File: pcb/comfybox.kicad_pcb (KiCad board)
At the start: 2 copper layers, 0 parts

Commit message: finished pcb without oled
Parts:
- added DOWN1: SW_CHOC, Kailh:Kailh_socket_PG1350_optional, F.Cu at (85.1, 61.3)
- added K1: SW_CHOC, Kailh:Kailh_socket_PG1350_optional, F.Cu at (155.0, 98.3)
- added K2: SW_CHOC, Kailh:Kailh_socket_PG1350_optional, F.Cu at (175.9, 78.7)
- added K3: SW_CHOC, Kailh:Kailh_socket_PG1350_optional, F.Cu at (204.0, 71.7)
- added K4: SW_CHOC, Kailh:Kailh_socket_PG1350_optional, F.Cu at (232.9, 71.7)
- added LEFT1: SW_CHOC, Kailh:Kailh_socket_PG1350_optional, F.Cu at (57.0, 54.3)
- added OPT1: SW_Push, Button_Switch_THT:SW_PUSH_6mm, F.Cu at (42.8, 35.2)
- added OPT2: SW_Push, Button_Switch_THT:SW_PUSH_6mm, F.Cu at (54.8, 35.2)
- added OPT3: SW_Push, Button_Switch_THT:SW_PUSH_6mm, F.Cu at (66.8, 35.2)
- added OPT4: SW_Push, Button_Switch_THT:SW_PUSH_6mm, F.Cu at (78.8, 35.2)
- added OPT5: SW_Push, Button_Switch_THT:SW_PUSH_6mm, F.Cu at (90.8, 35.2)
- added P1: SW_CHOC, Kailh:Kailh_socket_PG1350_optional, F.Cu at (150.0, 70.2)
- added P2: SW_CHOC, Kailh:Kailh_socket_PG1350_optional, F.Cu at (170.9, 50.6)
- added P3: SW_CHOC, Kailh:Kailh_socket_PG1350_optional, F.Cu at (199.0, 43.5)
- added P4: SW_CHOC, Kailh:Kailh_socket_PG1350_optional, F.Cu at (227.9, 43.5)
- added RIGHT1: SW_CHOC, Kailh:Kailh_socket_PG1350_optional, F.Cu at (106.0, 81.0)
- added RPZ1: RP2040-Zero, RP2040-Zero:RP2040-Zero, F.Cu at (130.1, 35.0)
- added UP1: SW_CHOC, Kailh:Kailh_socket_PG1350_optional, F.Cu at (106.0, 130.0)
- added UP2: SW_CHOC, Kailh:Kailh_socket_PG1350_optional, F.Cu at (150.0, 130.0)
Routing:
- net K4: track 0.00 -> 141.3 mm
- net UP L: track 0.00 -> 113.2 mm
- net UP R: track 0.00 -> 112.4 mm
- net P4: track 0.00 -> 109.9 mm
- net K3: track 0.00 -> 104.2 mm
- net START: track 0.00 -> 87.7 mm
- net LEFT: track 0.00 -> 83.5 mm
- net K1: track 0.00 -> 79.8 mm
- net P3: track 0.00 -> 79.0 mm
- net K2: track 0.00 -> 77.8 mm
- net SELECT: track 0.00 -> 74.7 mm
- net RIGHT: track 0.00 -> 63.2 mm
- net HOME: track 0.00 -> 61.6 mm
- net DOWN: track 0.00 -> 61.6 mm
- net P2: track 0.00 -> 51.6 mm
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- added copper zone on B.Cu, net GND
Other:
- board outline added: 242 x 138 mm

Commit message: add oled
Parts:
- added OLED1: SSD1306, SSD1306:128x64OLED, F.Cu at (135.0, 102.0)
- moved OPT1 19.0 mm to (61.8, 35.2)
- moved OPT2 19.0 mm to (73.8, 35.2)
- moved OPT3 19.0 mm to (85.8, 35.2)
- moved OPT4 19.0 mm to (97.8, 35.2)
- moved OPT5 19.0 mm to (109.8, 35.2)
- moved K1 12.0 mm to (167.0, 98.3)
- moved K2 12.0 mm to (187.9, 78.7)
- moved K3 12.0 mm to (216.0, 71.7)
- moved K4 12.0 mm to (244.9, 71.7)
- moved P1 12.0 mm to (162.0, 70.2)
- moved P2 12.0 mm to (182.9, 50.6)
- moved P3 12.0 mm to (211.0, 43.5)
- moved P4 12.0 mm to (239.9, 43.5)
- moved UP2 12.0 mm to (162.0, 130.0)
- moved RPZ1 4.91 mm to (135.0, 35.0)
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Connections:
- RPZ1 pad 21: +3.3V -> 3V3
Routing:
- net OLED SDA: track 0.00 -> 74.9 mm, vias 0 -> 4
- net 3V3: track 0.00 -> 73.5 mm, vias 0 -> 4
- net OLED SCL: track 0.00 -> 71.3 mm, vias 0 -> 4
- net LEFT: track 83.5 -> 105.6 mm
- net K4: track 141.3 -> 163.1 mm
- net P4: track 109.9 -> 131.0 mm
- net K3: track 104.2 -> 124.9 mm
- net K1: track 79.8 -> 98.9 mm
- net UP L: track 113.2 -> 131.4 mm
- net UP R: track 112.4 -> 129.0 mm
- net RIGHT: track 63.2 -> 79.6 mm
- net P3: track 79.0 -> 95.3 mm
- net P1: track 51.4 -> 67.1 mm
- net K2: track 77.8 -> 92.3 mm
- net START: track 87.7 -> 73.6 mm
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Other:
- outline, holes or cut-outs redrawn

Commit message: adjust tracing
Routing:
- net P1: track 67.1 -> 71.7 mm
- net UP R: track 129.0 -> 126.7 mm
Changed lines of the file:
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@@
   (gr_line (start 142 23) (end 257 23) (layer "Edge.Cuts") (width 0.1))
   (gr_line (start 128 44.485516) (end 128 23) (layer "Edge.Cuts") (width 0.1))
-  (segment (start 144 76) (end 144 45.305516) (width 0.25) (layer "F.Cu") (net 1))
-  (segment (start 150 82) (end 144 76) (width 0.25) (layer "F.Cu") (net 1))
-  (segment (start 156.095571 82) (end 150 82) (width 0.25) (layer "F.Cu") (net 1))
+  (segment (start 147.272792 81.5) (end 139.518198 73.745406) (width 0.25) (layer "F.Cu") (net 1))
+  (segment (start 144 46.5) (end 144 45.305516) (width 0.25) (layer "F.Cu") (net 1))
   (segment (start 144 45.305516) (end 144.16 45.145516) (width 0.25) (layer "F.Cu") (net 1))
-  (segment (start 162.00027 76.095301) (end 156.095571 82) (width 0.25) (layer "F.Cu") (net 1))
+  (segment (start 139.518198 50.981802) (end 144 46.5) (width 0.25) (layer "F.Cu") (net 1))
+  (segment (start 156.595571 81.5) (end 147.272792 81.5) (width 0.25) (layer "F.Cu") (net 1))
+  (segment (start 162.00027 76.095301) (end 156.595571 81.5) (width 0.25) (layer "F.Cu") (net 1))
+  (segment (start 139.518198 73.745406) (end 139.518198 50.981802) (width 0.25) (layer "F.Cu") (net 1))
   (segment (start 158.76027 72.820301) (end 162.03527 76.095301) (width 0.25) (layer "B.Cu") (net 1))
   (segment (start 158.76027 64.245301) (end 158.76027 72.820301) (width 0.25) (layer "B.Cu") (net 1))
@@
   (segment (start 236.631082 46.172382) (end 239.906082 49.447382) (width 0.25) (layer "B.Cu") (net 5))
   (segment (start 236.631082 37.597382) (end 236.631082 46.172382) (width 0.25) (layer "B.Cu") (net 5))
-  (segment (start 150 84) (end 140 74) (width 0.25) (layer "F.Cu") (net 6))
-  (segment (start 140 74) (end 140 46.765516) (width 0.25) (layer "F.Cu") (net 6))
-  (segment (start 140 46.765516) (end 140.08 46.685516) (width 0.25) (layer "F.Cu") (net 6))
-  (segment (start 152 110) (end 150 108) (width 0.25) (layer "F.Cu") (net 6))
+  (segment (start 150 84.863604) (end 139.068198 73.931802) (width 0.25) (layer "F.Cu") (net 6))
+  (segment (start 152.5 110) (end 150 107.5) (width 0.25) (layer "F.Cu") (net 6))
   (segment (start 167.00027 104.233869) (end 161.234139 110) (width 0.25) (layer "F.Cu") (net 6))
-  (segment (start 161.234139 110) (end 152 110) (width 0.25) (layer "F.Cu") (net 6))
-  (segment (start 150 108) (end 150 84) (width 0.25) (layer "F.Cu") (net 6))
+  (segment (start 139.068198 50.511802) (end 140.08 49.5) (width 0.25) (layer "F.Cu") (net 6))
+  (segment (start 161.234139 110) (end 152.5 110) (width 0.25) (layer "F.Cu") (net 6))
+  (segment (start 150 107.5) (end 150 84.863604) (width 0.25) (layer "F.Cu") (net 6))
+  (segment (start 140.08 49.5) (end 140.08 46.685516) (width 0.25) (layer "F.Cu") (net 6))
+  (segment (start 139.068198 73.931802) (end 139.068198 50.5) (width 0.25) (layer "F.Cu") (net 6))
   (segment (start 163.76027 100.958869) (end 167.03527 104.233869) (width 0.25) (layer "B.Cu") (net 6))
   (segment (start 163.76027 92.383869) (end 163.76027 100.958869) (width 0.25) (layer "B.Cu") (net 6))
@@
   (segment (start 103.725 132.625) (end 107 135.9) (width 0.25) (layer "B.Cu") (net 13))
   (segment (start 103.725 124.05) (end 103.725 132.625) (width 0.25) (layer "B.Cu") (net 13))
-  (segment (start 162 135.9) (end 154.9 143) (width 0.25) (layer "F.Cu") (net 14))
-  (segment (start 149 85) (end 137.54 73.54) (width 0.25) (layer "F.Cu") (net 14))
-  (segment (start 154.9 143) (end 151 143) (width 0.25) (layer "F.Cu") (net 14))
-  (segment (start 137.54 73.54) (end 137.54 46.685516) (width 0.25) (layer "F.Cu") (net 14))
-  (segment (start 149 141) (end 149 85) (width 0.25) (layer "F.Cu") (net 14))
-  (segment (start 151 143) (end 149 141) (width 0.25) (layer "F.Cu") (net 14))
+  (segment (start 149.5 139.5) (end 149.5 85) (width 0.25) (layer "F.Cu") (net 14))
+  (segment (start 137.5 46.725516) (end 137.54 46.685516) (width 0.25) (layer "F.Cu") (net 14))
+  (segment (start 162 135.9) (end 156.4 141.5) (width 0.25) (layer "F.Cu") (net 14))
+  (segment (start 149.5 85) (end 138.5 74) (width 0.25) (layer "F.Cu") (net 14))
+  (segment (start 138.5 74) (end 138.5 50.5) (width 0.25) (layer "F.Cu") (net 14))
+  (segment (start 156.4 141.5) (end 151.5 141.5) (width 0.25) (layer "F.Cu") (net 14))
+  (segment (start 138.5 50.5) (end 137.5 49.5) (width 0.25) (layer "F.Cu") (net 14))
+  (segment (start 151.5 141.5) (end 149.5 139.5) (width 0.25) (layer "F.Cu") (net 14))
+  (segment (start 137.5 49.5) (end 137.5 46.725516) (width 0.25) (layer "F.Cu") (net 14))
   (segment (start 158.725 132.625) (end 162 135.9) (width 0.25) (layer "B.Cu") (net 14))
   (segment (start 158.725 124.05) (end 158.725 132.625) (width 0.25) (layer "B.Cu") (net 14))

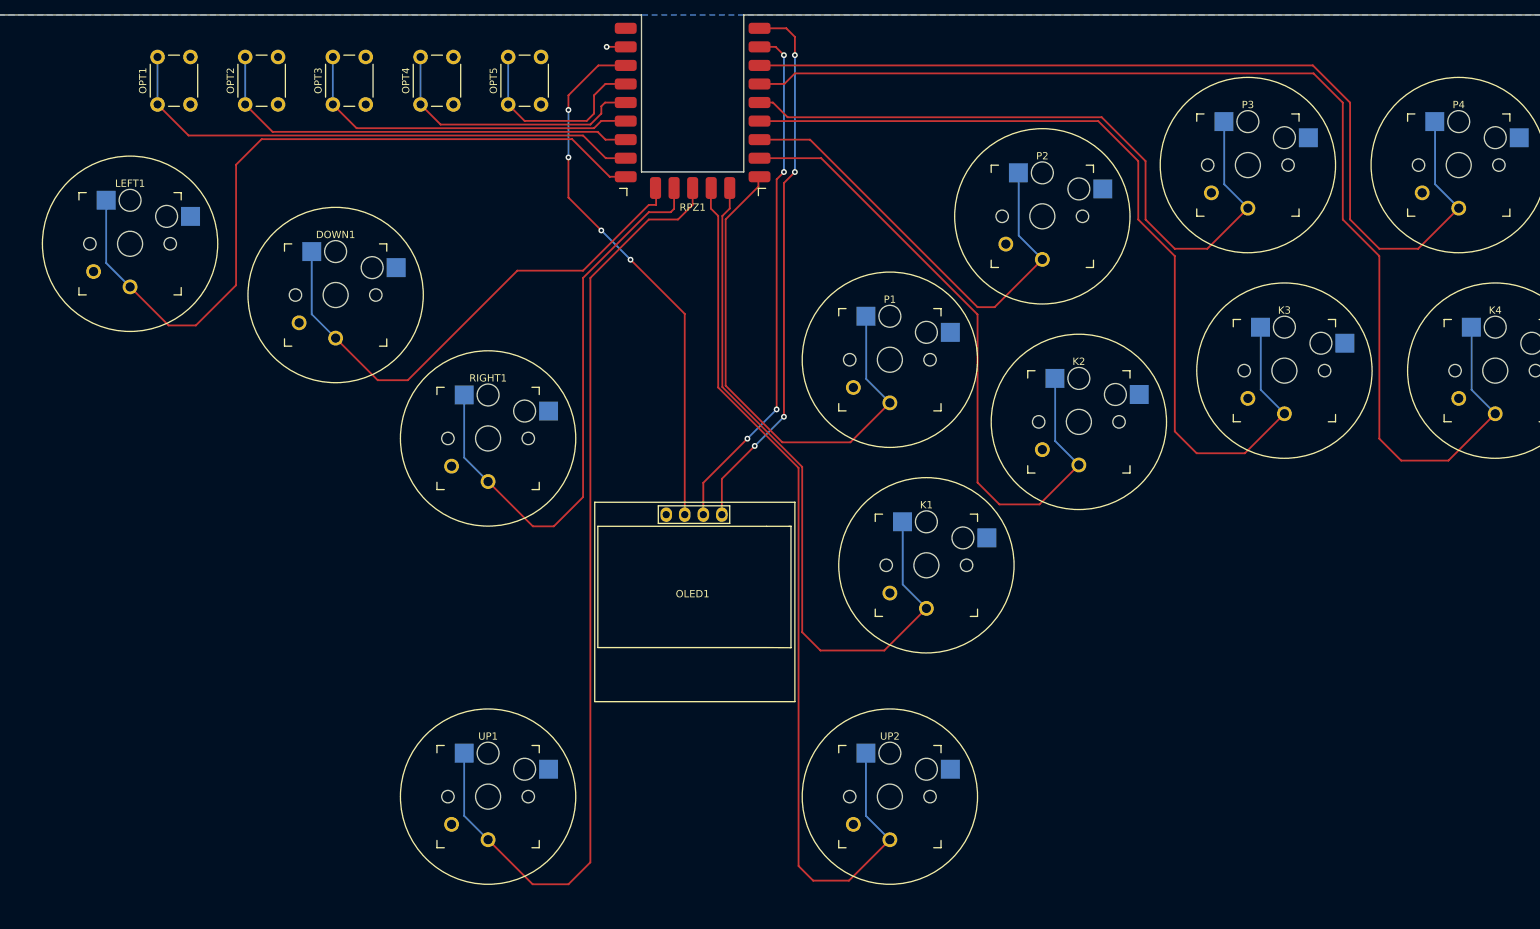
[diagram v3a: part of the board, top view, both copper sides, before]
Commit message: improve spacing and redo tracing
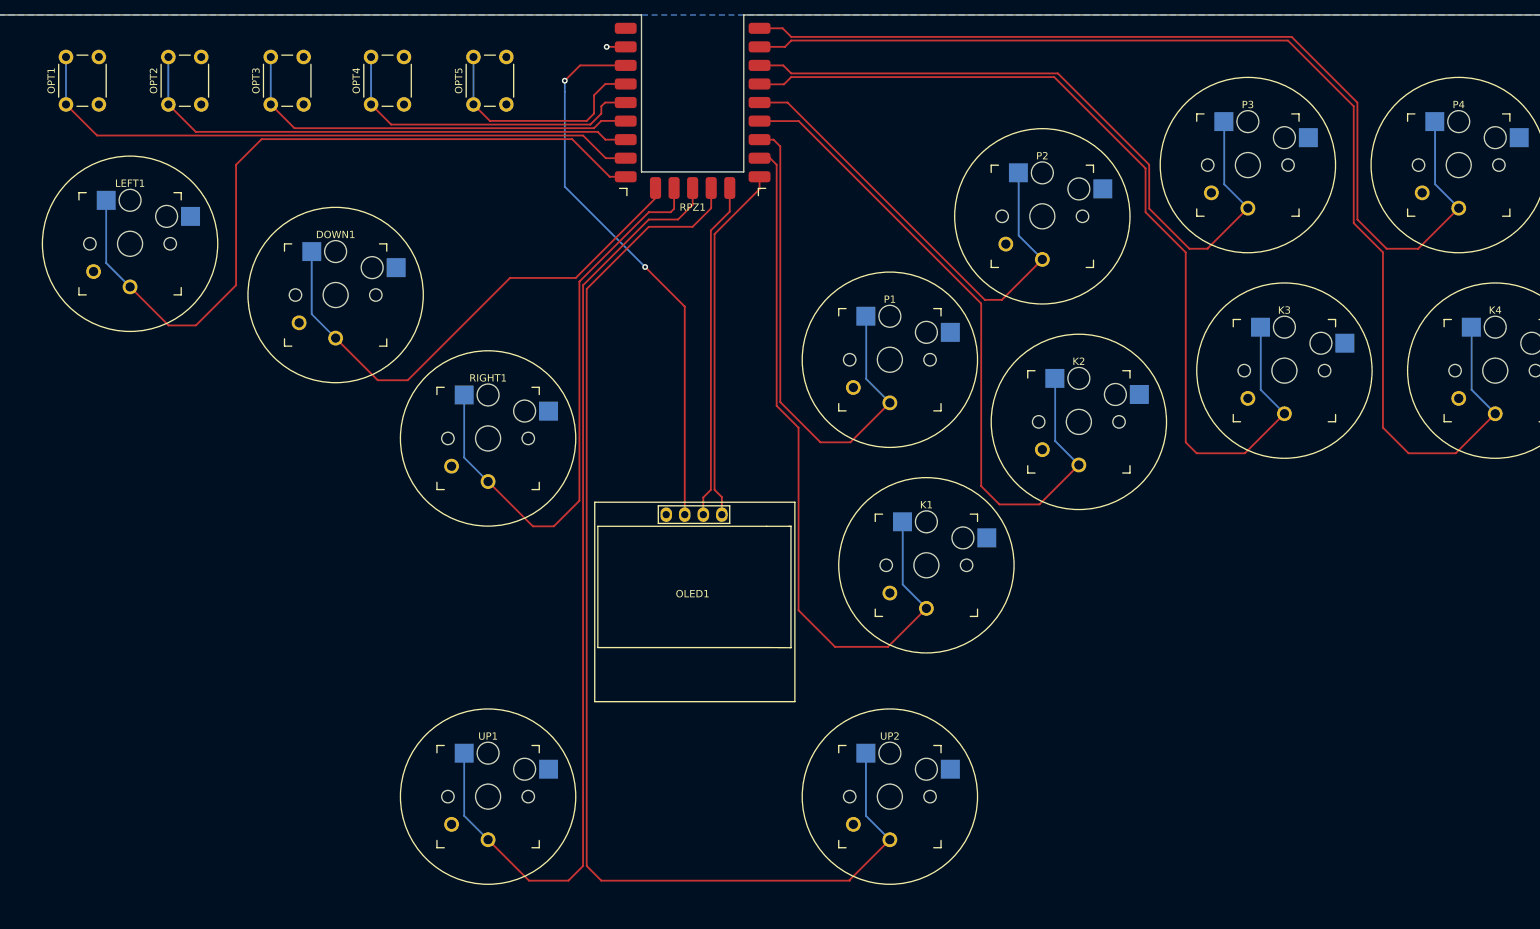
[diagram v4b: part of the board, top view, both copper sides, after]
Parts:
- moved OPT1 12.5 mm to (49.2, 35.2)
- moved OPT2 10.5 mm to (63.2, 35.2)
- moved OPT3 8.50 mm to (77.2, 35.2)
- moved OPT4 6.77 mm to (91.0, 35.2)
- moved OPT5 4.75 mm to (105.0, 35.2)
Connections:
- RPZ1 pad 1: OLED SDA -> P4
- RPZ1 pad 10: K1 -> OLED SCL
- RPZ1 pad 2: OLED SCL -> K4
- RPZ1 pad 3: P4 -> P3
- RPZ1 pad 4: K4 -> K3
- RPZ1 pad 5: P3 -> P2
- RPZ1 pad 6: K3 -> K2
- RPZ1 pad 7: P2 -> P1
- RPZ1 pad 8: K2 -> K1
- RPZ1 pad 9: P1 -> OLED SDA
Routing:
- net UP R: track 126.7 -> 161.3 mm
- net OLED SDA: track 74.9 -> 49.2 mm, vias 4 -> 0
- net OLED SCL: track 71.3 -> 46.2 mm, vias 4 -> 0
- net START: track 73.6 -> 86.2 mm
- net SELECT: track 60.6 -> 71.1 mm
- net HOME: track 48.4 -> 56.9 mm
- net R3: track 37.6 -> 44.3 mm
- net L3: track 27.1 -> 31.8 mm
- net K2: track 92.3 -> 95.5 mm
- net K3: track 124.9 -> 127.8 mm
- net P4: track 131.0 -> 133.1 mm
- net 3V3: track 73.5 -> 75.4 mm, vias 4 -> 2
- net P2: track 64.1 -> 65.4 mm
- net P3: track 95.3 -> 96.3 mm
- net P1: track 71.7 -> 71.0 mm
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
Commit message: wip adjusted angle
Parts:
- moved UP1 8.00 mm to (107.0, 138.0)
- moved UP2 8.00 mm to (162.0, 138.0)
- moved OLED1 7.65 mm to (135.0, 109.7)
- moved RIGHT1 3.50 mm to (107.0, 84.5)
- moved DOWN1 2.19 mm to (86.5, 63.5)
- moved K4 1.80 mm to (245.5, 70.0)
- moved K3 1.76 mm to (216.5, 70.0)
- moved LEFT1 1.75 mm to (58.5, 56.0)
- moved P3 1.63 mm to (210.5, 42.0)
- moved P4 1.59 mm to (239.5, 42.0)
- moved K2 1.36 mm to (188.5, 77.5)
- moved P2 1.13 mm to (182.5, 49.5)
- moved K1 1.01 mm to (168.0, 98.5)
- moved P1 0.30 mm to (162.0, 70.5)
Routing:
- net LEFT: track 105.6 -> 70.1 mm
- net UP R: track 161.3 -> 169.3 mm
- net UP L: track 130.7 -> 138.7 mm
- net OLED SDA: track 49.2 -> 56.9 mm
- net OLED SCL: track 46.2 -> 53.9 mm
- net 3V3: track 75.4 -> 83.1 mm
- net K4: track 163.4 -> 161.5 mm
- net L3: track 31.8 -> 30.4 mm
- net K2: track 95.5 -> 94.1 mm
- net P3: track 96.3 -> 97.0 mm
- net R3: track 44.3 -> 43.7 mm

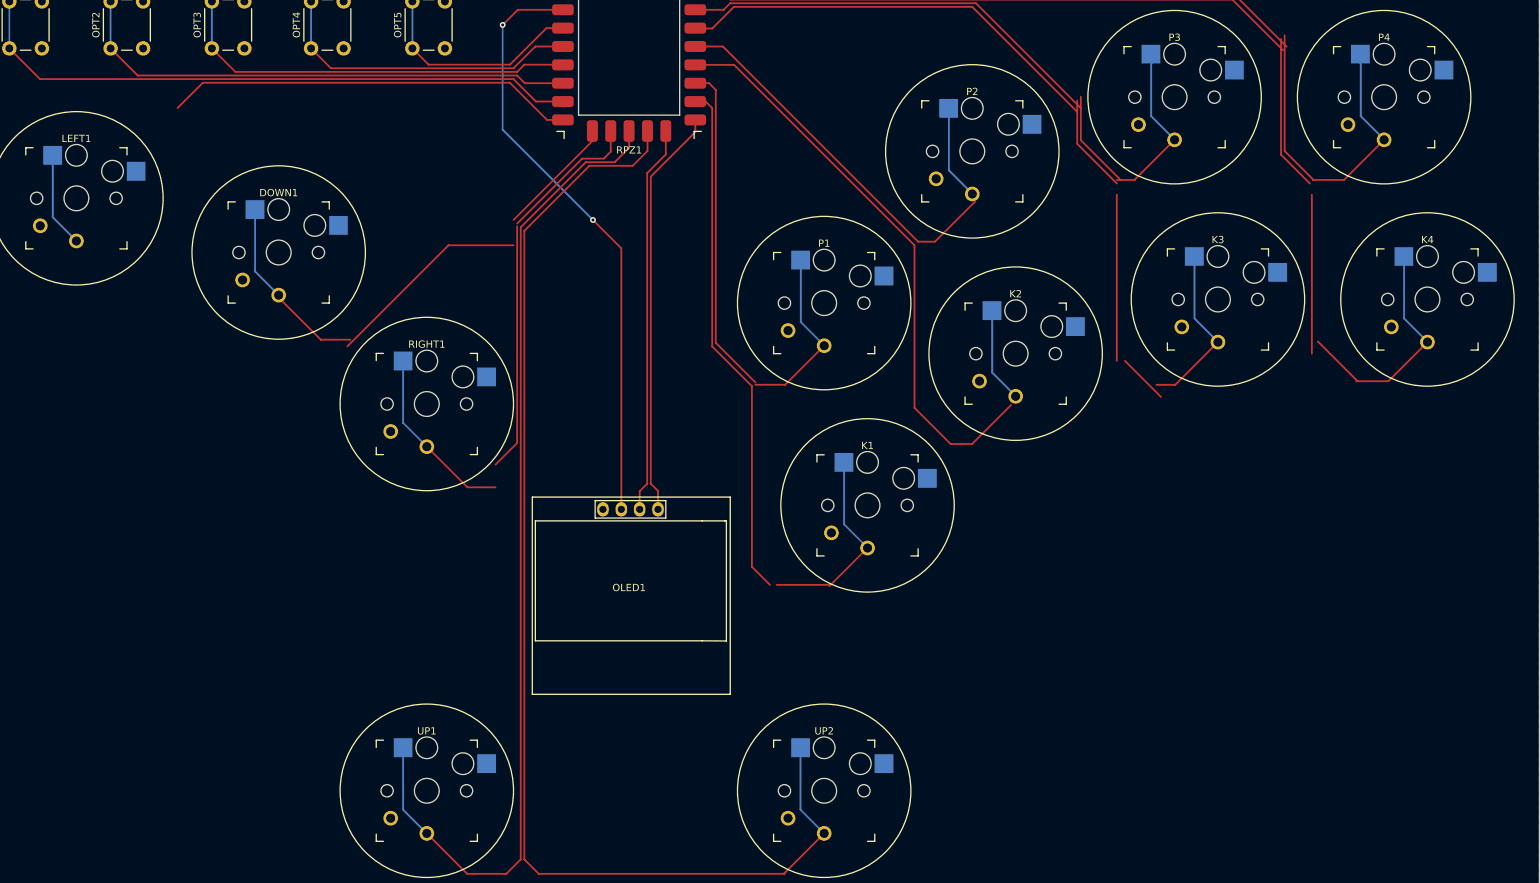
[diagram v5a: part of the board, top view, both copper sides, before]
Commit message: update libs and add KS33 support
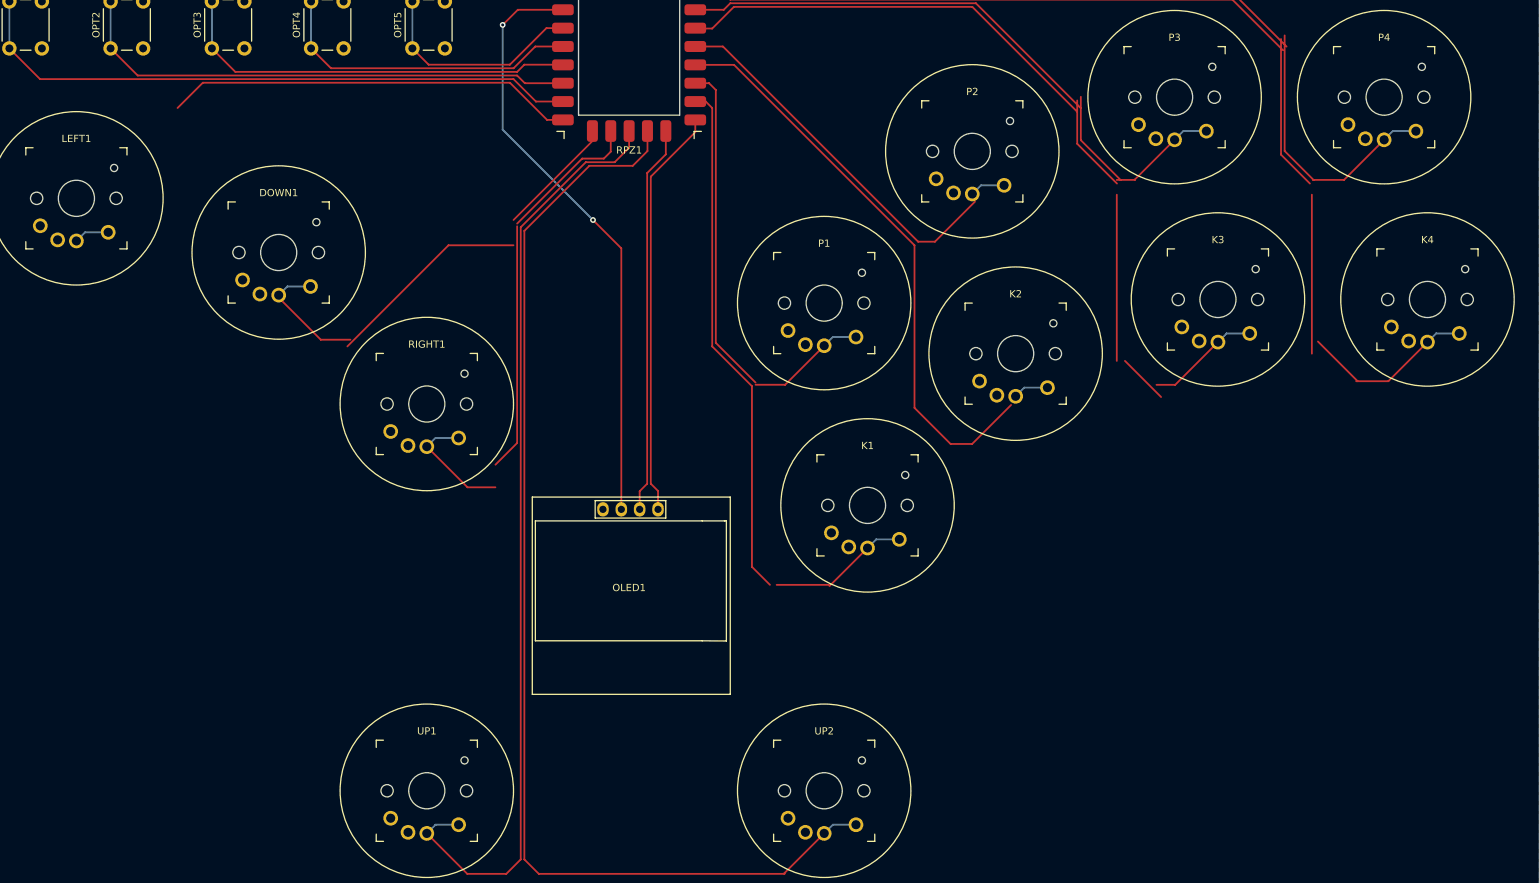
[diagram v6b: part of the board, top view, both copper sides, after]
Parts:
- DOWN1, K1, K2, K3, K4, LEFT1, P1, P2, P3, P4, RIGHT1, UP1, UP2: footprint Kailh:Kailh_socket_PG1350_optional -> Switch:Kailh_PG1350_Gateron_KS27_KS33
- OLED1: footprint SSD1306:128x64OLED -> OLED:SSD1306-128x64_OLED
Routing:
- net K4: track 161.5 -> 46.8 mm
- net P4: track 133.1 -> 231.1 mm
- net K3: track 128.1 -> 45.9 mm
- net P3: track 97.0 -> 162.6 mm
- net P2: track 65.4 -> 57.1 mm
- net LEFT: track 70.1 -> 61.8 mm
- net DOWN: track 71.2 -> 62.9 mm
- net RIGHT: track 79.2 -> 70.9 mm
- net P1: track 71.0 -> 62.6 mm
- net K2: track 94.1 -> 85.8 mm
- net K1: track 99.9 -> 91.6 mm
- net UP R: track 169.3 -> 161.0 mm
- net UP L: track 138.7 -> 130.4 mm

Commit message: cleanup
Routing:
- net P4: track 231.1 -> 91.0 mm
- net P3: track 162.6 -> 64.6 mm
- net K4: track 46.8 -> 89.6 mm
- net RIGHT: track 70.9 -> 28.4 mm
- net DOWN: track 62.9 -> 27.1 mm
- net K3: track 45.9 -> 65.0 mm
- net K2: track 85.8 -> 68.1 mm
- net K1: track 91.6 -> 76.9 mm
- net P1: track 62.6 -> 50.9 mm
- net P2: track 57.1 -> 46.9 mm
- net UP R: track 161.0 -> 157.5 mm
- net UP L: track 130.4 -> 128.1 mm
- net 3V3: track 83.1 -> 83.8 mm, vias 2 -> 4

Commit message: layout experiments
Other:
- board size 242 x 138 mm -> 240 x 130 mm
